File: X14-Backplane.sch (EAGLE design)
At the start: 34 parts, among them J2 PXC-PTSM-04-RA-1778641, J3 PXC-8-RA-1778683, J8 PXC-8-RA-1778683

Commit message: STEPS!
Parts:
- DIST_TO_BACKPLANE: device Samtec MPPT Hermaphoditic 10 pos - MPPT-10-01-01-L-RA-SD:MPPT-10-01-01-L-RA-SD -> CONN, Samtec MPPT Hermaphoditic 10 pos - MPPT-10-01-01-L-RA-SD:MPPT-10-01-01-L-RA-SD
- J2: device Phoenix Contact PTSM-04-V-1778573:PXC-PTSM-04-RA-1778641 -> CONN, Phoenix Contact PTSM-04-V-1778573:PXC-PTSM-04-RA-1778641
- J3, J8: device Phoenix Contact PTSM 8 pin:PXC-8-RA-1778683 -> CONN, Phoenix Contact PTSM 8 pin:PXC-8-RA-1778683
- U$1, U$2, U$3: device BLHeli_32 45A:BACKPLANE_CONNECTORSBKP -> Conn, Backplane-ESC-Controller:BACKPLANE_CONNECTORSBKP
- U$5, U$6, U$7: device Backplane_ESC_adapter:BACKPLANE_ESC_ADAPTER_PWRBKP -> CONN, Backplane_ESC_adapter:BACKPLANE_ESC_ADAPTER_PWRBKP
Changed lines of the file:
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@@
 <part name="FRAME2" library="SparkFun-Aesthetics" library_urn="urn:adsk.eagle:library:507" deviceset="FRAME-A4L" device=""/>
 <part name="MUX" library="BackplaneMUX" deviceset="TI-SN74LV4052A" device=""/>
-<part name="J2" library="Phoenix Contact PTSM-04-V-1778573" deviceset="PXC-PTSM-04-RA-1778641" device=""/>
-<part name="J3" library="Phoenix Contact PTSM 8 pin" deviceset="PXC-8-RA-1778683" device="" package3d_urn="urn:adsk.eagle:package:25224885/2"/>
+<part name="J2" library="CONN, Phoenix Contact PTSM-04-V-1778573" deviceset="PXC-PTSM-04-RA-1778641" device="" package3d_urn="urn:adsk.eagle:package:33723680/2"/>
+<part name="J3" library="CONN, Phoenix Contact PTSM 8 pin" deviceset="PXC-8-RA-1778683" device="" package3d_urn="urn:adsk.eagle:package:25224885/2"/>
 <part name="R4" library="SparkFun-Resistors" library_urn="urn:adsk.eagle:library:532" deviceset="26.7KOHM" device="0603-1/10W-1%" package3d_urn="urn:adsk.eagle:package:39650/1" value="22k"/>
 <part name="R1" library="SparkFun-Resistors" library_urn="urn:adsk.eagle:library:532" deviceset="10KOHM" device="-0603-1/10W-1%" package3d_urn="urn:adsk.eagle:package:39650/1" value="10k"/>
 <part name="R5" library="SparkFun-Resistors" library_urn="urn:adsk.eagle:library:532" deviceset="1KOHM" device="-0603-1/10W-1%" package3d_urn="urn:adsk.eagle:package:39650/1" value="4.7k"/>
-<part name="DIST_TO_BACKPLANE" library="Samtec MPPT Hermaphoditic 10 pos - MPPT-10-01-01-L-RA-SD" deviceset="MPPT-10-01-01-L-RA-SD" device="" package3d_urn="urn:adsk.eagle:package:25115828/2"/>
+<part name="DIST_TO_BACKPLANE" library="CONN, Samtec MPPT Hermaphoditic 10 pos - MPPT-10-01-01-L-RA-SD" deviceset="MPPT-10-01-01-L-RA-SD" device="" package3d_urn="urn:adsk.eagle:package:25115828/2"/>
 <part name="H1" library="Mounting Holes" deviceset="6-32-HOLE" device="" package3d_urn="urn:adsk.eagle:package:24384748/2"/>
 <part name="H2" library="Mounting Holes" deviceset="6-32-HOLE" device="" package3d_urn="urn:adsk.eagle:package:24384748/2"/>
-<part name="U$5" library="Backplane_ESC_adapter" deviceset="BACKPLANE_ESC_ADAPTER_PWR" device="BKP"/>
-<part name="U$6" library="Backplane_ESC_adapter" deviceset="BACKPLANE_ESC_ADAPTER_PWR" device="BKP"/>
-<part name="U$7" library="Backplane_ESC_adapter" deviceset="BACKPLANE_ESC_ADAPTER_PWR" device="BKP"/>
-<part name="U$1" library="BLHeli_32 45A" deviceset="BACKPLANE_CONNECTORS" device="BKP"/>
-<part name="U$2" library="BLHeli_32 45A" deviceset="BACKPLANE_CONNECTORS" device="BKP"/>
-<part name="U$3" library="BLHeli_32 45A" deviceset="BACKPLANE_CONNECTORS" device="BKP"/>
+<part name="U$5" library="CONN, Backplane_ESC_adapter" deviceset="BACKPLANE_ESC_ADAPTER_PWR" device="BKP" package3d_urn="urn:adsk.eagle:package:33723362/2" value="BACKPLANE_ESC_ADAPTER_PWRBKP"/>
+<part name="U$6" library="CONN, Backplane_ESC_adapter" deviceset="BACKPLANE_ESC_ADAPTER_PWR" device="BKP" package3d_urn="urn:adsk.eagle:package:33723362/2" value="BACKPLANE_ESC_ADAPTER_PWRBKP"/>
+<part name="U$7" library="CONN, Backplane_ESC_adapter" deviceset="BACKPLANE_ESC_ADAPTER_PWR" device="BKP" package3d_urn="urn:adsk.eagle:package:33723362/2" value="BACKPLANE_ESC_ADAPTER_PWRBKP"/>
+<part name="U$1" library="Conn, Backplane-ESC-Controller" deviceset="BACKPLANE_CONNECTORS" device="BKP" package3d_urn="urn:adsk.eagle:package:33721620/2"/>
+<part name="U$2" library="Conn, Backplane-ESC-Controller" deviceset="BACKPLANE_CONNECTORS" device="BKP" package3d_urn="urn:adsk.eagle:package:33721620/2"/>
+<part name="U$3" library="Conn, Backplane-ESC-Controller" deviceset="BACKPLANE_CONNECTORS" device="BKP" package3d_urn="urn:adsk.eagle:package:33721620/2"/>
 <part name="R7" library="SparkFun-Resistors" library_urn="urn:adsk.eagle:library:532" deviceset="68.1KOHM" device="-0603-1/10W-1%" package3d_urn="urn:adsk.eagle:package:39650/1" value="60"/>
 <part name="R8" library="SparkFun-Resistors" library_urn="urn:adsk.eagle:library:532" deviceset="68.1KOHM" device="-0603-1/10W-1%" package3d_urn="urn:adsk.eagle:package:39650/1" value="60"/>
@@
 <part name="U$8" library="OTHER, Push button - FSM2JMTR" deviceset="DISCRETECOMPONENTS_SWITCH" device="" package3d_urn="urn:adsk.eagle:package:24384574/2"/>
 <part name="R9" library="SparkFun-Resistors" library_urn="urn:adsk.eagle:library:532" deviceset="10KOHM" device="-0603-1/10W-1%" package3d_urn="urn:adsk.eagle:package:39650/1" value="10k"/>
-<part name="U$4" library="CONN, Distribution-Backplane" deviceset="BACKPLANE-DISTRIBUTION" device=""/>
-<part name="J8" library="Phoenix Contact PTSM 8 pin" deviceset="PXC-8-RA-1778683" device="" package3d_urn="urn:adsk.eagle:package:25224885/2"/>
-<part name="U$9" library="PI-SHIELD, Solenoid-Backplane" deviceset="7X_CONN" device=""/>
-<part name="U$10" library="CONN, DataConversion-Backplane Connector- SAMTEC CLT-107-01-F-D" deviceset="BACKPLANE-&gt;DATACONV" device=""/>
+<part name="U$4" library="CONN, Distribution-Backplane" deviceset="BACKPLANE-DISTRIBUTION" device="" package3d_urn="urn:adsk.eagle:package:32878650/2"/>
+<part name="J8" library="CONN, Phoenix Contact PTSM 8 pin" deviceset="PXC-8-RA-1778683" device="" package3d_urn="urn:adsk.eagle:package:25224885/2"/>
+<part name="U$9" library="PI-SHIELD, Solenoid-Backplane" deviceset="7X_CONN" device="" package3d_urn="urn:adsk.eagle:package:33723615/2"/>
+<part name="U$10" library="CONN, DataConversion-Backplane Connector- SAMTEC CLT-107-01-F-D" deviceset="BACKPLANE-&gt;DATACONV" device="" package3d_urn="urn:adsk.eagle:package:33723582/2"/>
 <part name="C1" library="CAP, aluminin-capacitor-brick-UCM1H331MNL1GS" deviceset="UCM1H331MNL1GS" device="" package3d_urn="urn:adsk.eagle:package:24202090/2" value="330uF"/>
 <part name="C2" library="CAP, aluminin-capacitor-brick-UCM1H331MNL1GS" deviceset="UCM1H331MNL1GS" device="" package3d_urn="urn:adsk.eagle:package:24202090/2" value="330uF"/>

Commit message: new connector UwU SQT
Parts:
- removed U$1, U$2, U$3: BACKPLANE_CONNECTORSBKP, Conn, Backplane-ESC-Controller:BACKPLANE_CONNECTORSBKP
- added U$11, U$12, U$13: BACKPLANE_ESC, SQT-106-01-F-D:BACKPLANE_ESC
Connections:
- net 3V3: now also U$11.01, U$11.02, U$11.03, U$11.04, U$12.01, U$12.02, U$12.03, U$12.04, U$13.01, U$13.02, U$13.03, U$13.04; no longer U$1.1, U$1.2, U$1.3, U$1.4, U$2.1, U$2.2, U$2.3, U$2.4, U$3.1, U$3.2, U$3.3, U$3.4
- net CAN_H: now also U$11.05, U$12.05, U$13.05; no longer U$1.5, U$2.5, U$3.5
- net CAN_L: now also U$11.07, U$12.07, U$13.07; no longer U$1.7, U$2.7, U$3.7
- net ESCID_1: now also U$11.12; no longer U$1.12
- net ESCID_2: now also U$13.12; no longer U$2.12
- net ESCID_3: now also U$12.12; no longer U$3.12
- net GND_L: now also U$11.10, U$12.10, U$13.10; no longer U$1.10, U$2.10, U$3.10
- net NRST_1: now also U$11.06; no longer U$1.6
- net NRST_2: now also U$13.06; no longer U$2.6
- net NRST_3: now also U$12.06; no longer U$3.6
- net SWCLK_1: now also U$11.11; no longer U$1.11
- net SWCLK_2: now also U$13.11; no longer U$2.11
- net SWCLK_3: now also U$12.11; no longer U$3.11
- net SWDIO_1: now also U$11.09; no longer U$1.9
- net SWDIO_2: now also U$13.09; no longer U$2.9
- net SWDIO_3: now also U$12.09; no longer U$3.9
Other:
- moved on the sheet: R1, R4, R5

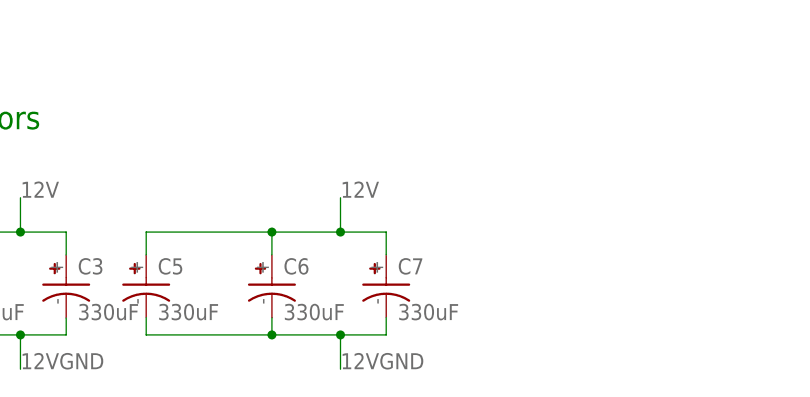
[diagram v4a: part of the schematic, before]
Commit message: shrunk board to better fit in box for v2
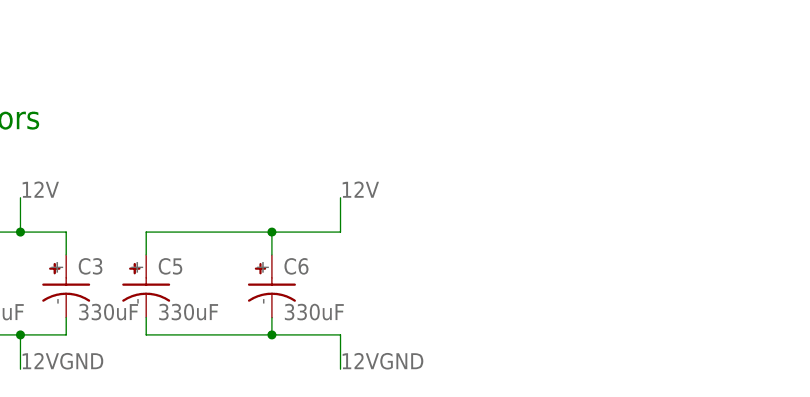
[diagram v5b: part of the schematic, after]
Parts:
- removed C7: 330uF, CAP, aluminin-capacitor-brick-UCM1H331MNL1GS:UCM1H331MNL1GS
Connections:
- net 12V: no longer C7.+
- net 12VGND: no longer C7.-
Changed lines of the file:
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@@
 <?xml version="1.0" encoding="utf-8"?>
 <!DOCTYPE eagle SYSTEM "eagle.dtd">
-<eagle version="9.6.2">
+<eagle version="9.5.0">
 <drawing>
 <settings>
@@
 <part name="C5" library="CAP, aluminin-capacitor-brick-UCM1H331MNL1GS" deviceset="UCM1H331MNL1GS" device="" package3d_urn="urn:adsk.eagle:package:24202090/2" value="330uF"/>
 <part name="C6" library="CAP, aluminin-capacitor-brick-UCM1H331MNL1GS" deviceset="UCM1H331MNL1GS" device="" package3d_urn="urn:adsk.eagle:package:24202090/2" value="330uF"/>
-<part name="C7" library="CAP, aluminin-capacitor-brick-UCM1H331MNL1GS" deviceset="UCM1H331MNL1GS" device="" package3d_urn="urn:adsk.eagle:package:24202090/2" value="330uF"/>
 <part name="U$12" library="SQT-106-01-F-D" deviceset="BACKPLANE_ESC" device=""/>
 <part name="U$13" library="SQT-106-01-F-D" deviceset="BACKPLANE_ESC" device=""/>
@@
 <attribute name="VALUE" x="189.23" y="-119.38" size="1.778" layer="95" align="center-left"/>
 </instance>
-<instance part="C7" gate="G$1" x="200.66" y="-115.57" smashed="yes">
-<attribute name="NAME" x="201.93" y="-114.3" size="1.778" layer="95" align="center-left"/>
-<attribute name="VALUE" x="201.93" y="-119.38" size="1.778" layer="95" align="center-left"/>
-</instance>
 <instance part="U$12" gate="G$1" x="93.98" y="140.97" smashed="yes">
 <attribute name="NAME" x="85.86" y="151.13" size="1.778" layer="95"/>
@@
 <wire x1="187.96" y1="-110.49" x2="195.58" y2="-110.49" width="0.1524" layer="91"/>
 <junction x="187.96" y="-110.49"/>
-<pinref part="C7" gate="G$1" pin="+"/>
-<wire x1="195.58" y1="-110.49" x2="200.66" y2="-110.49" width="0.1524" layer="91"/>
-<wire x1="200.66" y1="-110.49" x2="200.66" y2="-113.03" width="0.1524" layer="91"/>
 <wire x1="195.58" y1="-110.49" x2="195.58" y2="-106.68" width="0.1524" layer="91"/>
-<junction x="195.58" y="-110.49"/>
 <label x="195.58" y="-106.68" size="1.778" layer="95"/>
 </segment>
@@
 <wire x1="187.96" y1="-121.92" x2="195.58" y2="-121.92" width="0.1524" layer="91"/>
 <junction x="187.96" y="-121.92"/>
-<pinref part="C7" gate="G$1" pin="-"/>
-<wire x1="195.58" y1="-121.92" x2="200.66" y2="-121.92" width="0.1524" layer="91"/>
-<wire x1="200.66" y1="-121.92" x2="200.66" y2="-120.015" width="0.1524" layer="91"/>
 <wire x1="195.58" y1="-121.92" x2="195.58" y2="-125.73" width="0.1524" layer="91"/>
-<junction x="195.58" y="-121.92"/>
 <label x="195.58" y="-125.73" size="1.778" layer="95"/>
 </segment>
